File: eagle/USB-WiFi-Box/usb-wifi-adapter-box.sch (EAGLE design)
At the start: 8 parts

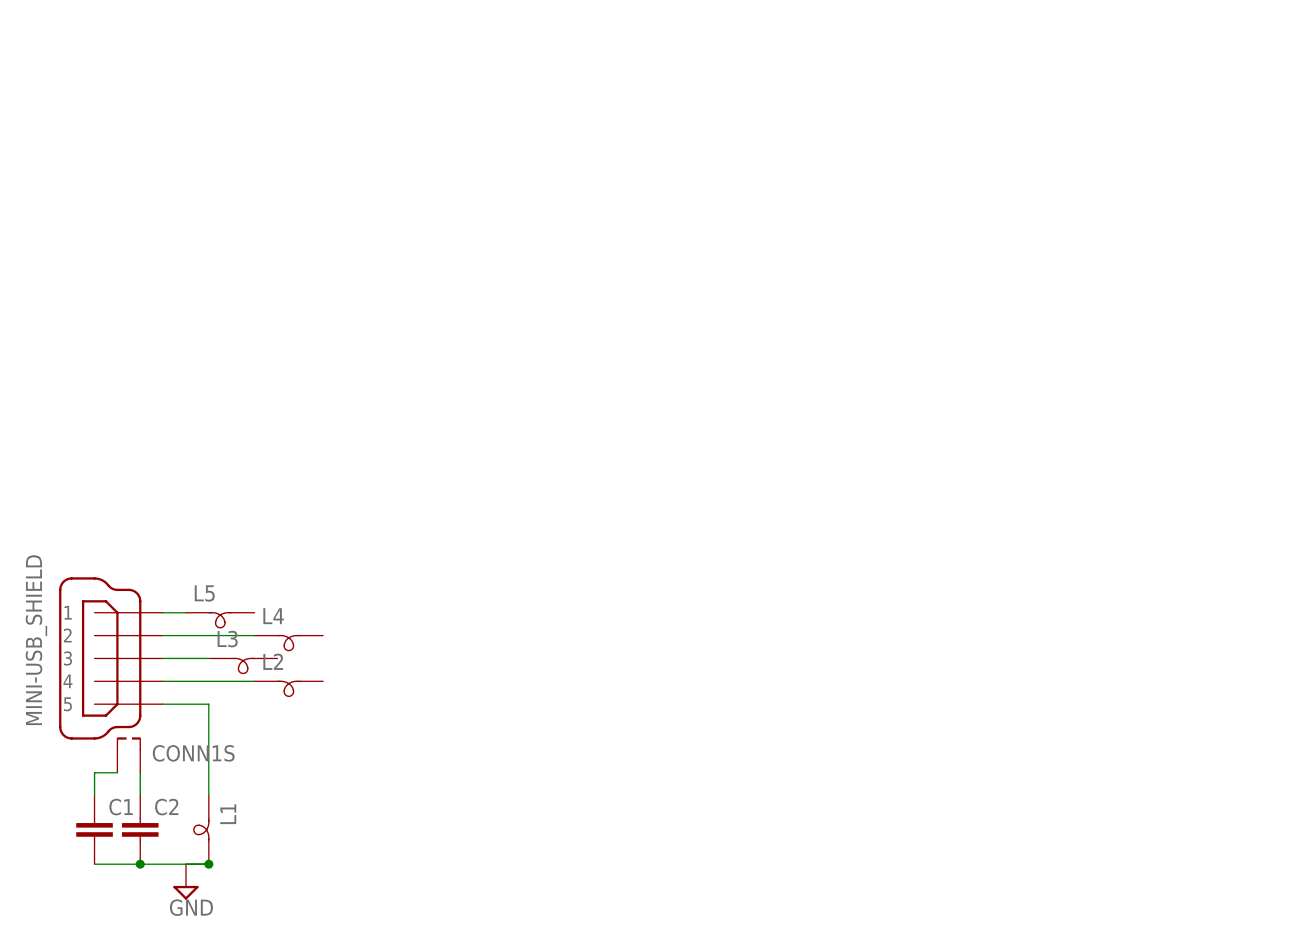
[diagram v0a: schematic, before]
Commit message: mounting holes in schematic and placeholder starter for wifi header
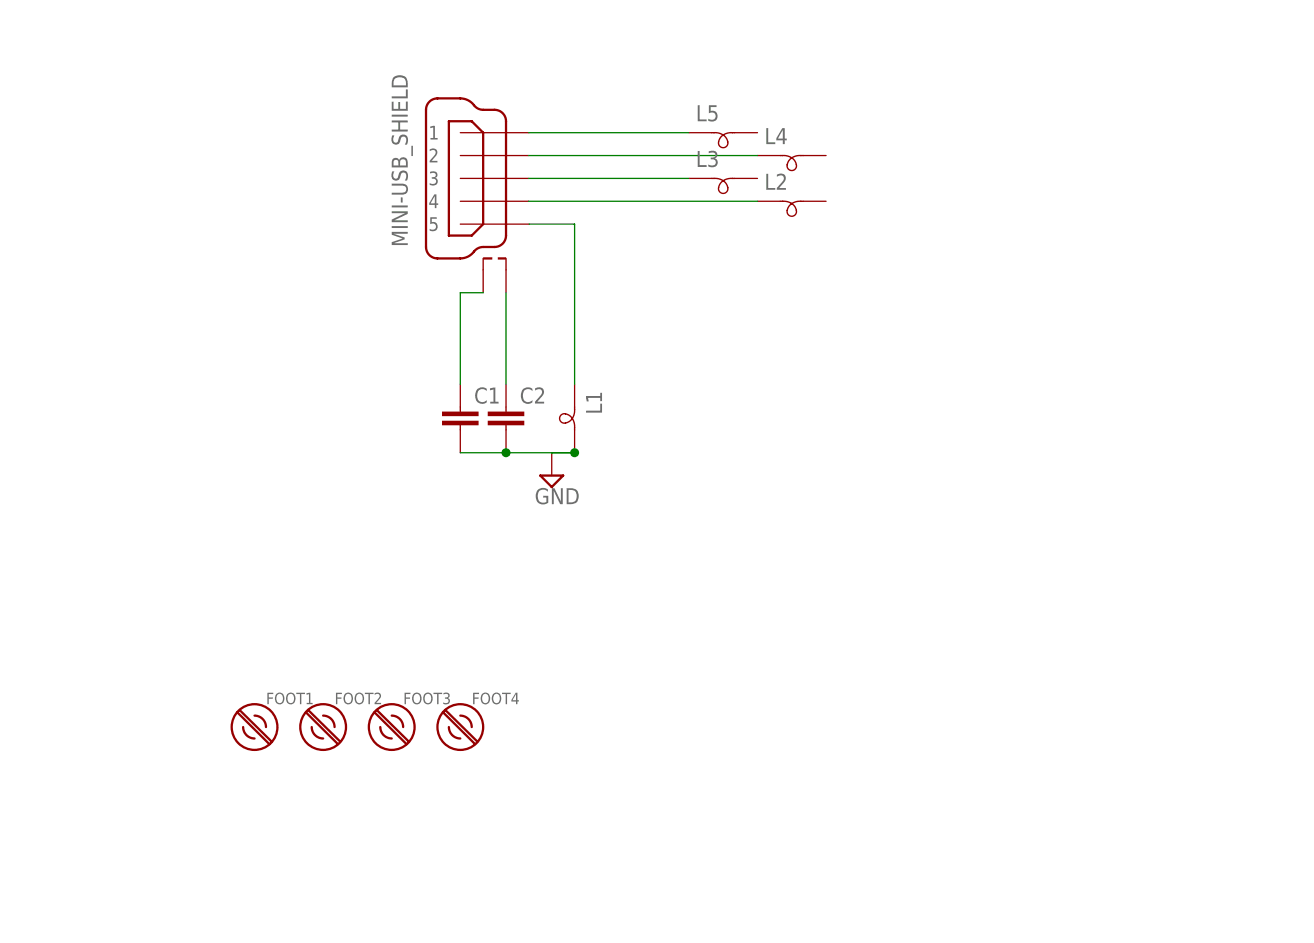
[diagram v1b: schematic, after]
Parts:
- added FOOT1, FOOT2, FOOT3, FOOT4: _4-BARE_MOUNTING_HOLE/.400, mount-2:_4-BARE_MOUNTING_HOLE/.400
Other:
- moved on the sheet: C1, C2, L1, L2, L3, L4, L5
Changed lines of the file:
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@@
 <layer number="48" name="Document" color="7" fill="1" visible="no" active="no"/>
 <layer number="49" name="Reference" color="7" fill="1" visible="no" active="no"/>
+<layer number="50" name="dxf" color="7" fill="1" visible="no" active="no"/>
 <layer number="51" name="tDocu" color="7" fill="1" visible="no" active="no"/>
 <layer number="52" name="bDocu" color="7" fill="1" visible="no" active="no"/>
+<layer number="53" name="tGND_GNDA" color="7" fill="1" visible="no" active="no"/>
+<layer number="54" name="bGND_GNDA" color="7" fill="1" visible="no" active="no"/>
+<layer number="56" name="wert" color="7" fill="1" visible="no" active="no"/>
 <layer number="91" name="Nets" color="2" fill="1" visible="yes" active="yes"/>
 <layer number="92" name="Busses" color="1" fill="1" visible="yes" active="yes"/>
@@
 <layer number="97" name="Info" color="7" fill="1" visible="yes" active="yes"/>
 <layer number="98" name="Guide" color="6" fill="1" visible="yes" active="yes"/>
+<layer number="100" name="Hidden_Layer" color="7" fill="1" visible="yes" active="yes"/>
+<layer number="101" name="Patch_Top" color="7" fill="1" visible="yes" active="yes"/>
+<layer number="102" name="Vscore" color="7" fill="1" visible="yes" active="yes"/>
+<layer number="103" name="tMap" color="7" fill="1" visible="yes" active="yes"/>
+<layer number="104" name="Name" color="7" fill="1" visible="yes" active="yes"/>
+<layer number="105" name="tPlate" color="7" fill="1" visible="yes" active="yes"/>
+<layer number="106" name="bPlate" color="7" fill="1" visible="yes" active="yes"/>
+<layer number="107" name="Crop" color="7" fill="1" visible="yes" active="yes"/>
+<layer number="116" name="Patch_BOT" color="7" fill="1" visible="yes" active="yes"/>
+<layer number="121" name="_tsilk" color="7" fill="1" visible="yes" active="yes"/>
+<layer number="122" name="_bsilk" color="7" fill="1" visible="yes" active="yes"/>
+<layer number="151" name="HeatSink" color="7" fill="1" visible="yes" active="yes"/>
+<layer number="200" name="200bmp" color="7" fill="1" visible="yes" active="yes"/>
+<layer number="201" name="201bmp" color="7" fill="1" visible="yes" active="yes"/>
+<layer number="202" name="202bmp" color="7" fill="1" visible="yes" active="yes"/>
+<layer number="203" name="203bmp" color="7" fill="1" visible="yes" active="yes"/>
+<layer number="204" name="204bmp" color="7" fill="1" visible="yes" active="yes"/>
+<layer number="205" name="205bmp" color="7" fill="1" visible="yes" active="yes"/>
+<layer number="206" name="206bmp" color="7" fill="1" visible="yes" active="yes"/>
+<layer number="207" name="207bmp" color="7" fill="1" visible="yes" active="yes"/>
+<layer number="208" name="208bmp" color="7" fill="1" visible="yes" active="yes"/>
+<layer number="215" name="ResistanceBottom" color="7" fill="1" visible="yes" active="yes"/>
+<layer number="250" name="Descript" color="7" fill="1" visible="yes" active="yes"/>
+<layer number="251" name="SMDround" color="7" fill="1" visible="yes" active="yes"/>
+<layer number="254" name="cooling" color="7" fill="1" visible="yes" active="yes"/>
 </layers>
 <schematic xreflabel="%F%N/%S.%C%R" xrefpart="/%S.%C%R">
@@
 <part name="C2" library="rcl" deviceset="C-EU" device="C0805"/>
 <part name="SUPPLY1" library="supply2" deviceset="GND" device=""/>
+<part name="FOOT1" library="mount-2" deviceset="_4-BARE_MOUNTING_HOLE" device="/.400"/>
+<part name="FOOT2" library="mount-2" deviceset="_4-BARE_MOUNTING_HOLE" device="/.400"/>
+<part name="FOOT3" library="mount-2" deviceset="_4-BARE_MOUNTING_HOLE" device="/.400"/>
+<part name="FOOT4" library="mount-2" deviceset="_4-BARE_MOUNTING_HOLE" device="/.400"/>
+<part name="FRAME1" library="frames" deviceset="A5L-LOC" device=""/>
 </parts>
 <sheets>
@@
 </plain>
 <instances>
-<instance part="CONN1" gate="G41" x="10.16" y="38.1" smashed="yes" rot="MR0">
-<attribute name="VALUE" x="0" y="30.48" size="1.778" layer="96" font="vector" rot="MR90"/>
+<instance part="CONN1" gate="G41" x="50.8" y="91.44" smashed="yes" rot="MR0">
+<attribute name="VALUE" x="40.64" y="83.82" size="1.778" layer="96" font="vector" rot="MR90"/>
 </instance>
-<instance part="L1" gate="G$1" x="20.32" y="17.78" rot="R270"/>
-<instance part="L2" gate="G$1" x="30.48" y="35.56"/>
-<instance part="L3" gate="G$1" x="25.4" y="38.1"/>
-<instance part="L4" gate="G$1" x="30.48" y="40.64"/>
-<instance part="L5" gate="G$1" x="22.86" y="43.18"/>
-<instance part="C1" gate="G$1" x="7.62" y="20.32"/>
-<instance part="C2" gate="G$1" x="12.7" y="20.32"/>
-<instance part="SUPPLY1" gate="GND" x="17.78" y="12.7"/>
-<instance part="CONN1" gate="S" x="12.7" y="27.94"/>
+<instance part="L1" gate="G$1" x="60.96" y="63.5" rot="R270"/>
+<instance part="L2" gate="G$1" x="86.36" y="88.9"/>
+<instance part="L3" gate="G$1" x="78.74" y="91.44"/>
+<instance part="L4" gate="G$1" x="86.36" y="93.98"/>
+<instance part="L5" gate="G$1" x="78.74" y="96.52"/>
+<instance part="C1" gate="G$1" x="48.26" y="66.04"/>
+<instance part="C2" gate="G$1" x="53.34" y="66.04"/>
+<instance part="SUPPLY1" gate="GND" x="58.42" y="58.42"/>
+<instance part="CONN1" gate="S" x="53.34" y="81.28" smashed="yes"/>
+<instance part="FOOT1" gate="MT" x="25.4" y="30.48" smashed="yes">
+<attribute name="NAME" x="26.67" y="33.02" size="1.27" layer="95"/>
+</instance>
+<instance part="FOOT2" gate="MT" x="33.02" y="30.48" smashed="yes">
+<attribute name="NAME" x="34.29" y="33.02" size="1.27" layer="95"/>
+</instance>
+<instance part="FOOT3" gate="MT" x="40.64" y="30.48" smashed="yes">
+<attribute name="NAME" x="41.91" y="33.02" size="1.27" layer="95"/>
+</instance>
+<instance part="FOOT4" gate="MT" x="48.26" y="30.48" smashed="yes">
+<attribute name="NAME" x="49.53" y="33.02" size="1.27" layer="95"/>
+</instance>
+<instance part="FRAME1" gate="G$1" x="0" y="0"/>
 </instances>
 <busses>
@@
 <pinref part="L2" gate="G$1" pin="1"/>
 <pinref part="CONN1" gate="G41" pin="4"/>
-<wire x1="15.24" y1="35.56" x2="25.4" y2="35.56" width="0.1524" layer="91"/>
+<wire x1="55.88" y1="88.9" x2="81.28" y2="88.9" width="0.1524" layer="91"/>
 </segment>
 </net>
@@
 <pinref part="CONN1" gate="G41" pin="3"/>
 <pinref part="L3" gate="G$1" pin="1"/>
-<wire x1="15.24" y1="38.1" x2="20.32" y2="38.1" width="0.1524" layer="91"/>
+<wire x1="55.88" y1="91.44" x2="73.66" y2="91.44" width="0.1524" layer="91"/>
 </segment>
 </net>
@@
 <pinref part="CONN1" gate="G41" pin="2"/>
 <pinref part="L4" gate="G$1" pin="1"/>
-<wire x1="15.24" y1="40.64" x2="25.4" y2="40.64" width="0.1524" layer="91"/>
+<wire x1="55.88" y1="93.98" x2="81.28" y2="93.98" width="0.1524" layer="91"/>
 </segment>
 </net>
@@
 <pinref part="CONN1" gate="G41" pin="1"/>
 <pinref part="L5" gate="G$1" pin="1"/>
-<wire x1="15.24" y1="43.18" x2="17.78" y2="43.18" width="0.1524" layer="91"/>
+<wire x1="55.88" y1="96.52" x2="73.66" y2="96.52" width="0.1524" layer="91"/>
 </segment>
 </net>
@@
 <pinref part="C1" gate="G$1" pin="2"/>
 <pinref part="C2" gate="G$1" pin="2"/>
-<wire x1="7.62" y1="15.24" x2="12.7" y2="15.24" width="0.1524" layer="91"/>
+<wire x1="48.26" y1="60.96" x2="53.34" y2="60.96" width="0.1524" layer="91"/>
 <pinref part="L1" gate="G$1" pin="2"/>
-<wire x1="12.7" y1="15.24" x2="20.32" y2="15.24" width="0.1524" layer="91"/>
-<junction x="12.7" y="15.24"/>
+<wire x1="53.34" y1="60.96" x2="60.96" y2="60.96" width="0.1524" layer="91"/>
+<junction x="53.34" y="60.96"/>
 <pinref part="SUPPLY1" gate="GND" pin="GND"/>
-<junction x="20.32" y="15.24"/>
-<wire x1="20.32" y1="15.24" x2="17.78" y2="15.24" width="0.1524" layer="91"/>
+<junction x="60.96" y="60.96"/>
+<wire x1="60.96" y1="60.96" x2="58.42" y2="60.96" width="0.1524" layer="91"/>
 </segment>
 </net>
@@
 <pinref part="CONN1" gate="G41" pin="5"/>
 <pinref part="L1" gate="G$1" pin="1"/>
-<wire x1="15.24" y1="33.02" x2="20.32" y2="33.02" width="0.1524" layer="91"/>
-<wire x1="20.32" y1="33.02" x2="20.32" y2="22.86" width="0.1524" layer="91"/>
+<wire x1="55.88" y1="86.36" x2="60.96" y2="86.36" width="0.1524" layer="91"/>
+<wire x1="60.96" y1="86.36" x2="60.96" y2="68.58" width="0.1524" layer="91"/>
 </segment>
 </net>
@@
 <pinref part="CONN1" gate="S" pin="S2"/>
 <pinref part="C2" gate="G$1" pin="1"/>
-<wire x1="12.7" y1="25.4" x2="12.7" y2="22.86" width="0.1524" layer="91"/>
+<wire x1="53.34" y1="78.74" x2="53.34" y2="68.58" width="0.1524" layer="91"/>
 </segment>
 </net>
@@
 <segment>
 <pinref part="CONN1" gate="S" pin="S1"/>
-<wire x1="10.16" y1="25.4" x2="7.62" y2="25.4" width="0.1524" layer="91"/>
+<wire x1="50.8" y1="78.74" x2="48.26" y2="78.74" width="0.1524" layer="91"/>
 <pinref part="C1" gate="G$1" pin="1"/>
-<wire x1="7.62" y1="25.4" x2="7.62" y2="22.86" width="0.1524" layer="91"/>
+<wire x1="48.26" y1="78.74" x2="48.26" y2="68.58" width="0.1524" layer="91"/>
 </segment>
 </net>
